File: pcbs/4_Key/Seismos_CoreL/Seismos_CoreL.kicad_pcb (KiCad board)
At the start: 2 copper layers, 147 x 78 mm, 26 parts, among them J1 SM09B-SRSS-TB(LF)(SN), J2 SM09B-SRSS-TB(LF)(SN), J3 SM09B-SRSS-TB(LF)(SN), J4 SM09B-SRSS-TB(LF)(SN), J5 SM09B-SRSS-TB(LF)(SN), J6 SM09B-SRSS-TB(LF)(SN), J7 Conn_01x05_Pin, J8 MJ-4PP-9-Lily58, J9 SM09B-SRSS-TB(LF)(SN), SW1 RotaryEncoder_Switch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

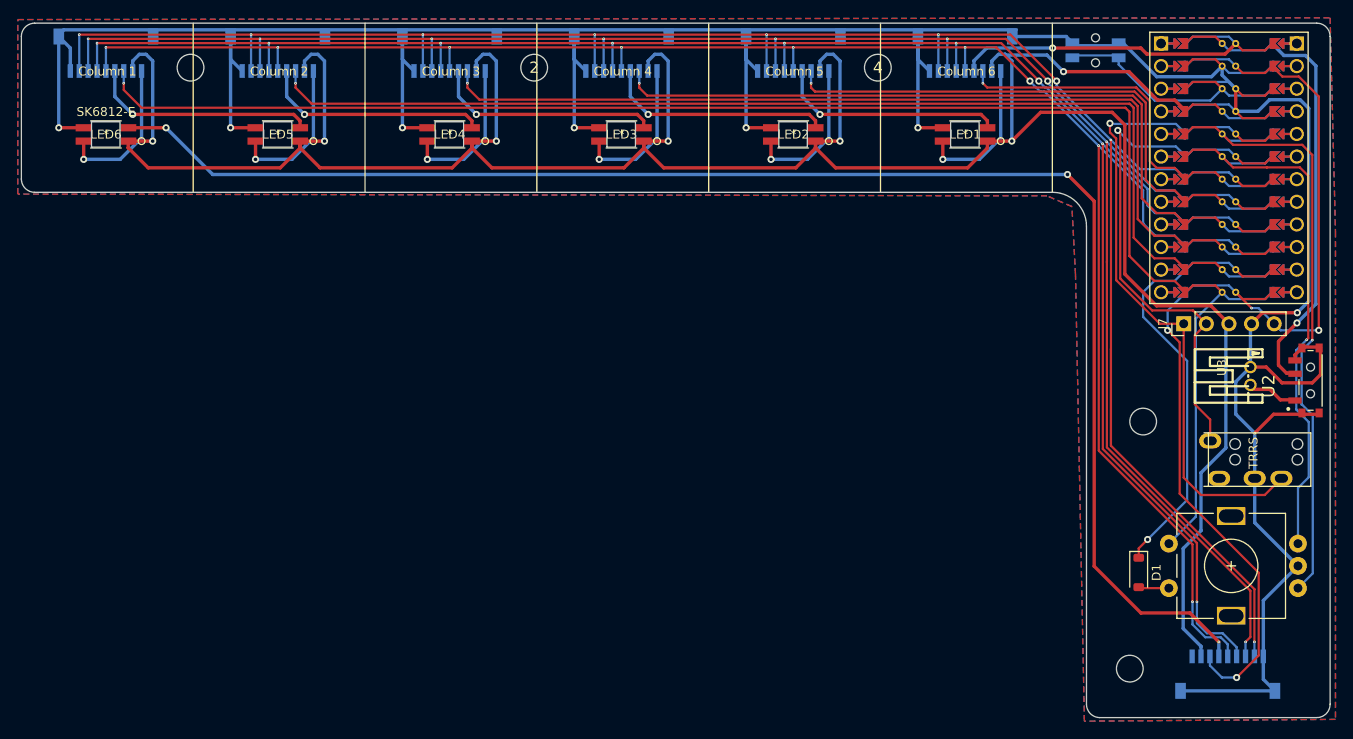
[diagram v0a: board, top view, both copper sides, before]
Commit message: Fix footprint errors and new 2x2 PCB
Fixed keyboard_reversible.pretty not being included.
Added a 2x2 PCB for the thumb.

Added a note regarding DRC errors involving two specific footprints...
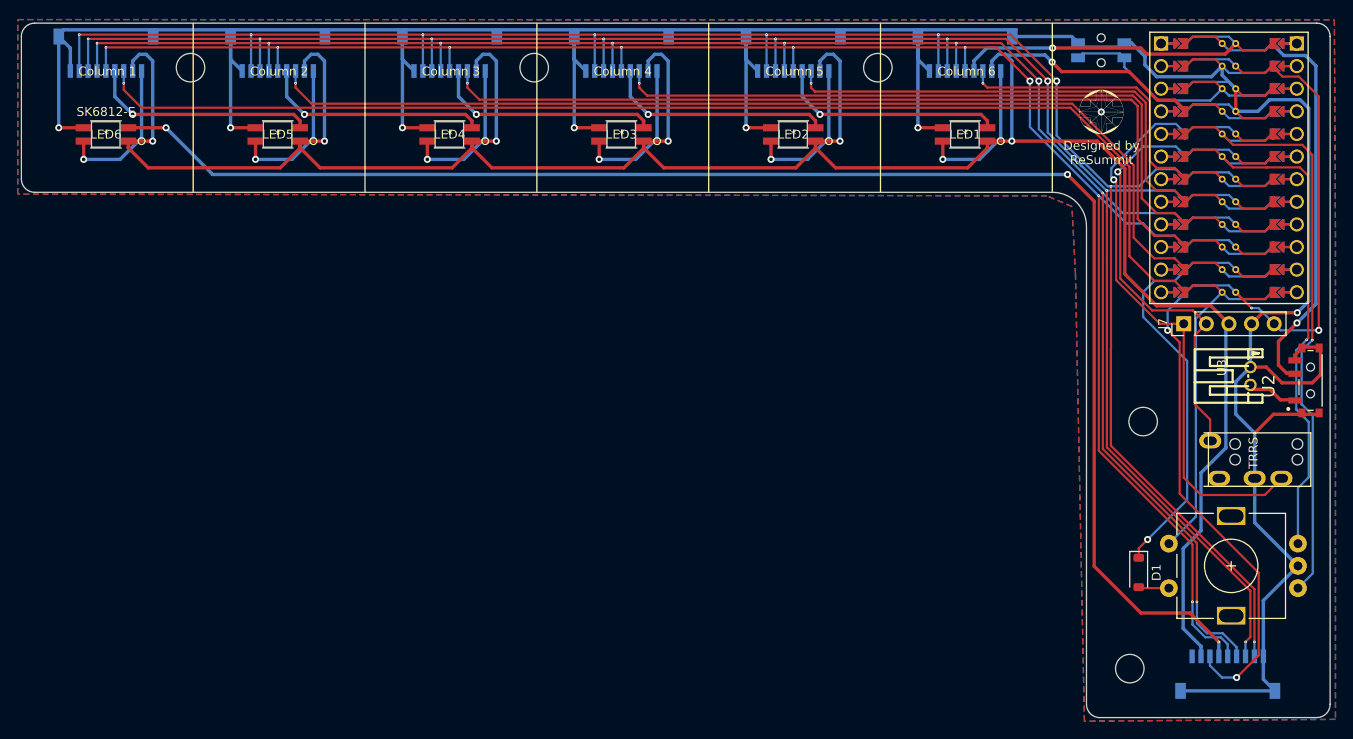
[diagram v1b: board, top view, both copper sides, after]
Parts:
- added G***: LOGO, Seismos-libs:ReSummit_Logo, F.Cu at (151.3, 30.0)
- 2, 4, ? (x3): value (none) -> Hole_M3_3.2mm; footprint (none) -> Seismos-libs:Hole_M3_3.2mm
- moved SW3 0.64 mm to (151.3, 23.0)
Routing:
- net /V+: track 316.6 -> 311.0 mm
- net /Row4: track 213.1 -> 208.3 mm
- net SCL: track 51.8 -> 47.6 mm
- net /Col_In5: track 118.9 -> 115.1 mm
- net /Col_In6: track 171.1 -> 167.4 mm
- net /Row3: track 215.5 -> 212.0 mm
- net SDA: track 66.4 -> 63.2 mm
- net /Row2: track 217.4 -> 215.2 mm
- net GND: track 364.9 -> 365.6 mm, vias 8 -> 9
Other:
- board text added: "Designed by ReSummit"
